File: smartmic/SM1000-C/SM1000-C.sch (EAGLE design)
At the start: 199 parts, among them CN1 HDR100-3, CN10 ST-3509, CN11 HDR100-3, CN12 DF11-16DS, CN2 MOLEX-MINI-B-SMT, CN3 RASM722PX, CN4 RJ-45, CN5 ST-3509, CN6 ST-3509, CN7 ST-3509, CN8 ST-3509, CN9 ST-3509, J1 JMP-2PIN, J3 JMP-2PIN, J4 JMP-2PIN, P1 TPAD50, P10 TPAD50, P11 TPAD50, P12 TPAD50, P13 TPAD50, P14 TPAD50, P15 TPAD50, P16 TPAD50, P17 TPAD50, P18 TPAD50, P19 TPAD50, P2 TPAD50, P20 TPAD50, P3 TPAD50, P4 TPAD50, P5 TPAD50, P6 TPAD50, P7 TPAD50, P8 TPAD50, P9 TPAD50, SW1 SW-BOURNS-7914S, SW2 SW-BOURNS-7914S, SW3 DPDT, SW4 SW-BOURNS-7914S, SW5 SW-BOURNS-7914J, T1 SM-LP-5001, T2 SM-LP-5001, U1 STM32F405, U2 LD3985M33R, U3 STMPS2141, U4 EMIF02-USB03F2, U5 TPS54329E, U6 LMV341, U7 LMV341, U8 LM386M-1, U9 LMV341

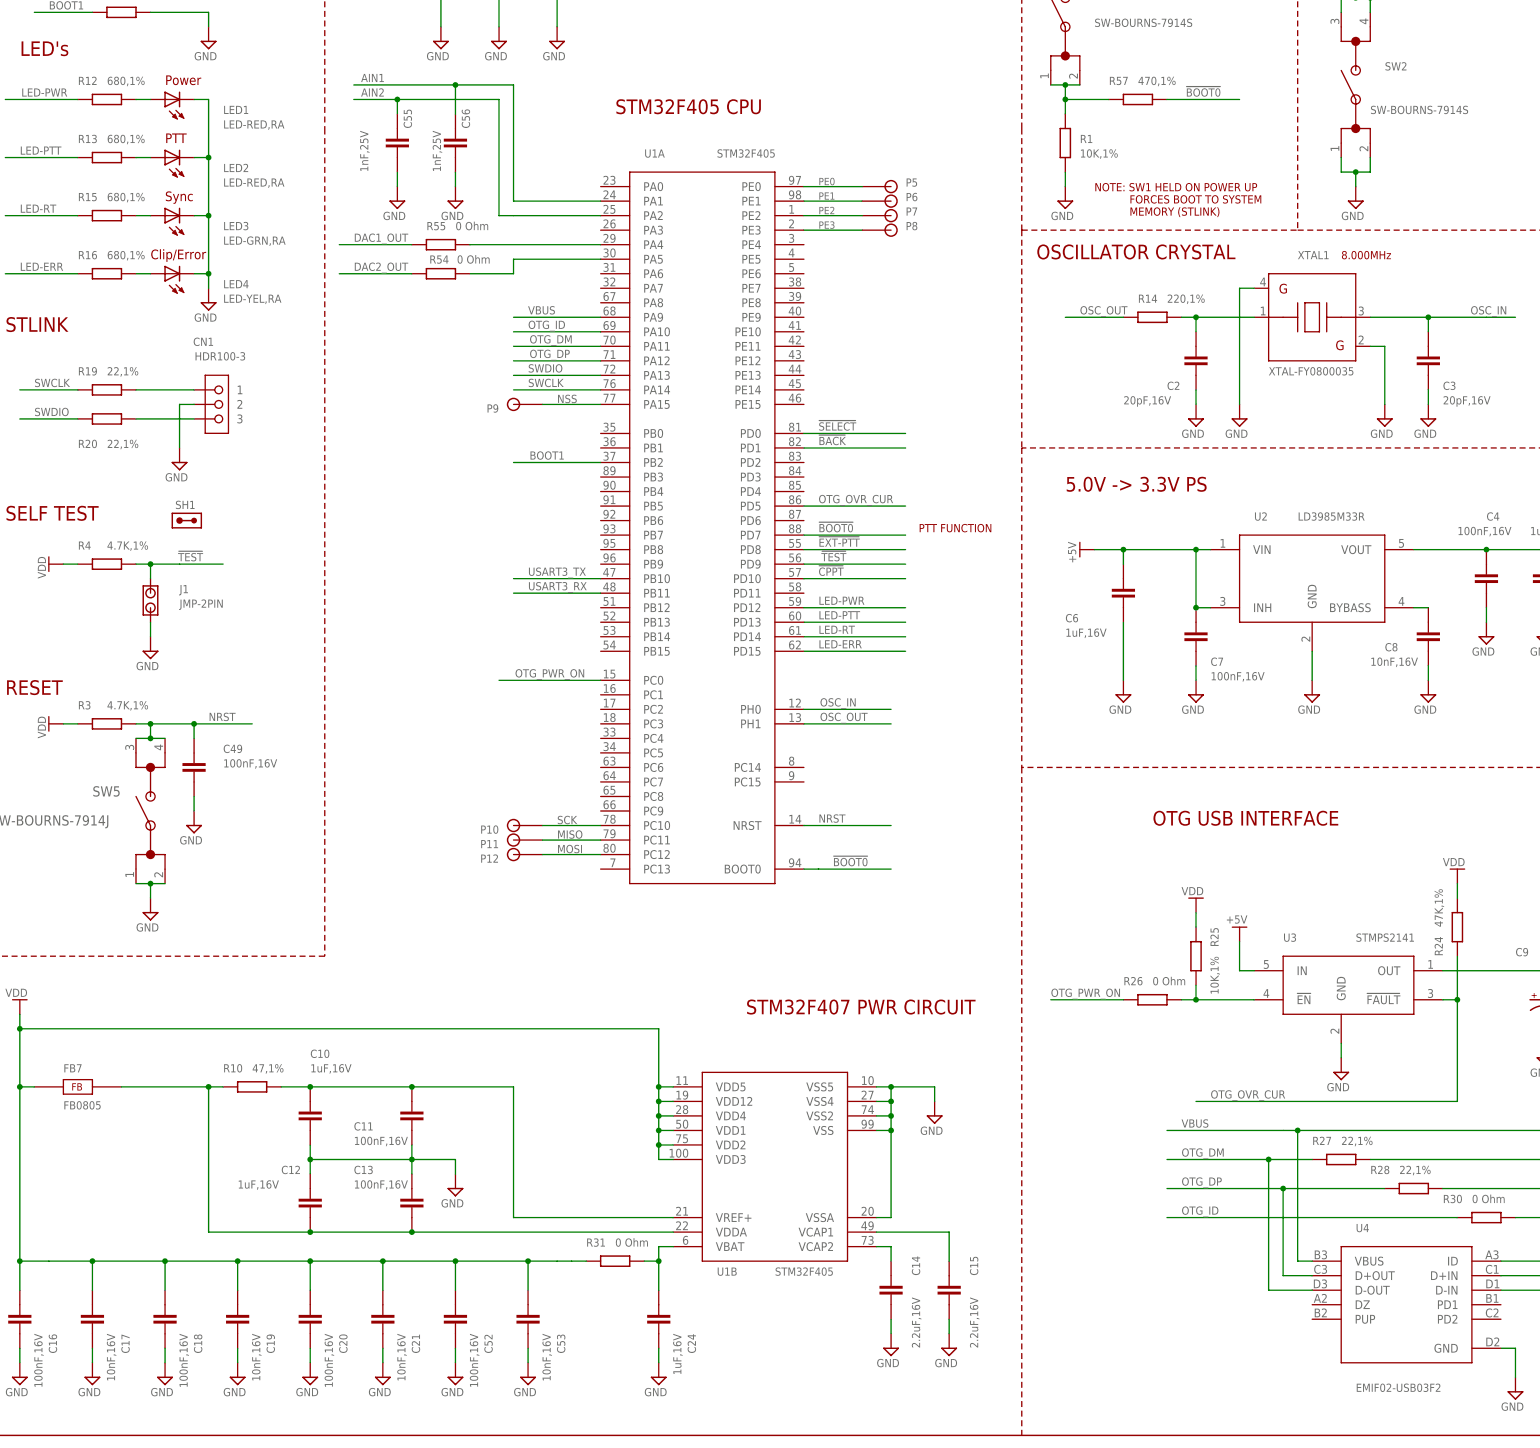
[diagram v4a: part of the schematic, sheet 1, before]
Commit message: Update schematics, PCB & BOM for addition of 0402 part footprints - RGB
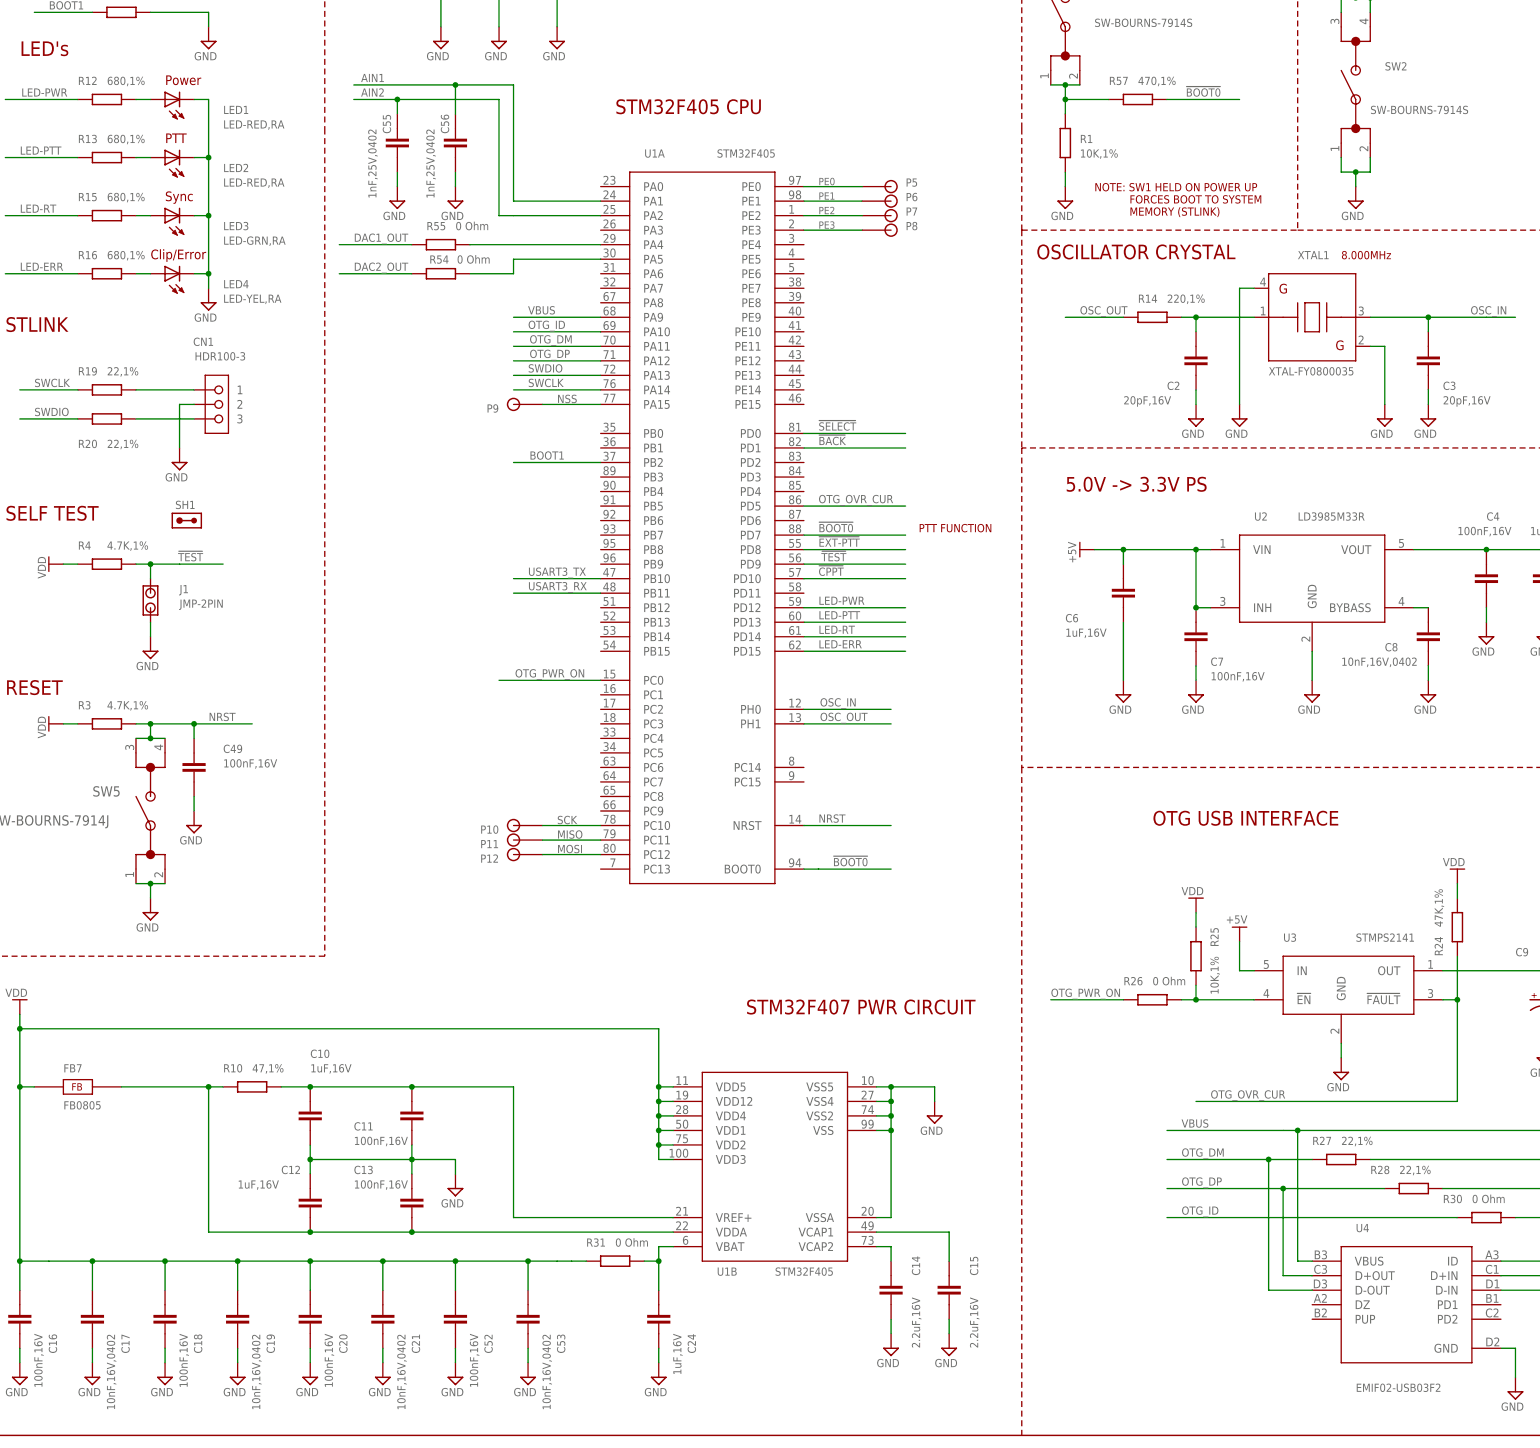
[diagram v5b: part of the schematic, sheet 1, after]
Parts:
- C1, C34, C55, C56: value 1nF,25V -> 1nF,25V,0402; device AA-ipc-7351-capacitor:CAPACITOR_0603 -> AA-ipc-7351-capacitor:CAPACITOR_0402
- C17, C19, C21, C53, C8: value 10nF,16V -> 10nF,16V,0402; device AA-ipc-7351-capacitor:CAPACITOR_0603 -> AA-ipc-7351-capacitor:CAPACITOR_0402
- C57: value 3.9nF,16V -> 3.9nF,16V,0402; device AA-ipc-7351-capacitor:CAPACITOR_0603 -> AA-ipc-7351-capacitor:CAPACITOR_0402
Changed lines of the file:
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@@
 <part name="V7" library="A-SUPPLY2" deviceset="GND" device=""/>
 <part name="V8" library="A-SUPPLY2" deviceset="GND" device=""/>
-<part name="C21" library="AA-ipc-7351-capacitor" deviceset="CAPACITOR_" device="0603" value="10nF,16V"/>
+<part name="C21" library="AA-ipc-7351-capacitor" deviceset="CAPACITOR_" device="0402" value="10nF,16V,0402"/>
 <part name="C20" library="AA-ipc-7351-capacitor" deviceset="CAPACITOR_" device="0603" value="100nF,16V"/>
-<part name="C19" library="AA-ipc-7351-capacitor" deviceset="CAPACITOR_" device="0603" value="10nF,16V"/>
+<part name="C19" library="AA-ipc-7351-capacitor" deviceset="CAPACITOR_" device="0402" value="10nF,16V,0402"/>
 <part name="C18" library="AA-ipc-7351-capacitor" deviceset="CAPACITOR_" device="0603" value="100nF,16V"/>
-<part name="C17" library="AA-ipc-7351-capacitor" deviceset="CAPACITOR_" device="0603" value="10nF,16V"/>
+<part name="C17" library="AA-ipc-7351-capacitor" deviceset="CAPACITOR_" device="0402" value="10nF,16V,0402"/>
 <part name="C16" library="AA-ipc-7351-capacitor" deviceset="CAPACITOR_" device="0603" value="100nF,16V"/>
 <part name="V9" library="A-SUPPLY2" deviceset="GND" device=""/>
@@
 <part name="V27" library="A-SUPPLY2" deviceset="+5V" device=""/>
 <part name="C5" library="AA-ipc-7351-capacitor" deviceset="CAPACITOR_" device="0603" value="1uF,16V"/>
-<part name="C8" library="AA-ipc-7351-capacitor" deviceset="CAPACITOR_" device="0603" value="10nF,16V"/>
+<part name="C8" library="AA-ipc-7351-capacitor" deviceset="CAPACITOR_" device="0402" value="10nF,16V,0402"/>
 <part name="C4" library="AA-ipc-7351-capacitor" deviceset="CAPACITOR_" device="0603" value="100nF,16V"/>
 <part name="V29" library="A-SUPPLY2" deviceset="GND" device=""/>
@@
 <part name="V55" library="A-SUPPLY2" deviceset="GND" device=""/>
 <part name="V56" library="A-SUPPLY2" deviceset="GND" device=""/>
-<part name="C34" library="AA-ipc-7351-capacitor" deviceset="CAPACITOR_" device="0603" value="1nF,25V"/>
+<part name="C34" library="AA-ipc-7351-capacitor" deviceset="CAPACITOR_" device="0402" value="1nF,25V,0402"/>
 <part name="R58" library="AA-ipc-7351-resistor" deviceset="RESISTOR_" device="0603" value="2.2K,1%"/>
 <part name="R40" library="AA-ipc-7351-resistor" deviceset="RESISTOR_" device="0603" value="2.2K,1%"/>
@@
 <part name="V71" library="A-SUPPLY2" deviceset="GND" device=""/>
 <part name="C52" library="AA-ipc-7351-capacitor" deviceset="CAPACITOR_" device="0603" value="100nF,16V"/>
-<part name="C53" library="AA-ipc-7351-capacitor" deviceset="CAPACITOR_" device="0603" value="10nF,16V"/>
+<part name="C53" library="AA-ipc-7351-capacitor" deviceset="CAPACITOR_" device="0402" value="10nF,16V,0402"/>
 <part name="V112" library="A-SUPPLY2" deviceset="GND" device=""/>
 <part name="V113" library="A-SUPPLY2" deviceset="GND" device=""/>
@@
 <part name="V123" library="A-SUPPLY2" deviceset="+5V" device=""/>
 <part name="U$3" library="A-SUPPLY2" deviceset="+VIN" device=""/>
-<part name="C1" library="AA-ipc-7351-capacitor" deviceset="CAPACITOR_" device="0603" value="1nF,25V"/>
+<part name="C1" library="AA-ipc-7351-capacitor" deviceset="CAPACITOR_" device="0402" value="1nF,25V,0402"/>
 <part name="V118" library="A-SUPPLY2" deviceset="GND" device=""/>
 <part name="C30" library="AA-ipc-7351-capacitor" deviceset="CAPACITOR_" device="0603" value="10nF,25V"/>
@@
 <part name="R55" library="AA-ipc-7351-resistor" deviceset="RESISTOR_" device="0805" value="0 Ohm"/>
 <part name="R54" library="AA-ipc-7351-resistor" deviceset="RESISTOR_" device="0805" value="0 Ohm"/>
-<part name="C55" library="AA-ipc-7351-capacitor" deviceset="CAPACITOR_" device="0603" value="1nF,25V"/>
-<part name="C56" library="AA-ipc-7351-capacitor" deviceset="CAPACITOR_" device="0603" value="1nF,25V"/>
+<part name="C55" library="AA-ipc-7351-capacitor" deviceset="CAPACITOR_" device="0402" value="1nF,25V,0402"/>
+<part name="C56" library="AA-ipc-7351-capacitor" deviceset="CAPACITOR_" device="0402" value="1nF,25V,0402"/>
 <part name="V125" library="A-SUPPLY2" deviceset="GND" device=""/>
 <part name="V126" library="A-SUPPLY2" deviceset="GND" device=""/>
@@
 <part name="V130" library="A-SUPPLY2" deviceset="GND" device=""/>
 <part name="R39" library="AA-ipc-7351-resistor" deviceset="RESISTOR_" device="1206" value="4.7,0.5W,1206"/>
-<part name="C57" library="AA-ipc-7351-capacitor" deviceset="CAPACITOR_" device="0603" value="3.9nF,16V"/>
+<part name="C57" library="AA-ipc-7351-capacitor" deviceset="CAPACITOR_" device="0402" value="3.9nF,16V,0402"/>
 <part name="V131" library="A-SUPPLY2" deviceset="GND" device=""/>
 <part name="R22" library="AA-ipc-7351-resistor" deviceset="RESISTOR_" device="0603" value="22.1K,1%"/>
@@
 <instance part="C8" gate="G$1" x="256.54" y="139.7" smashed="yes" rot="R270">
 <attribute name="NAME" x="248.92" y="137.16" size="1.4224" layer="95" ratio="9"/>
-<attribute name="VALUE" x="246.38" y="134.62" size="1.4224" layer="96" ratio="9"/>
+<attribute name="VALUE" x="241.3" y="134.62" size="1.4224" layer="96" ratio="9"/>
 </instance>
 <instance part="C4" gate="G$1" x="266.7" y="149.86" smashed="yes" rot="R270">
@@
 </instance>
 <instance part="C55" gate="G$1" x="76.2" y="226.06" smashed="yes" rot="R270">
-<attribute name="NAME" x="78.74" y="228.6" size="1.4224" layer="95" ratio="9" rot="R90"/>
-<attribute name="VALUE" x="71.12" y="220.98" size="1.4224" layer="96" ratio="9" rot="R90"/>
+<attribute name="NAME" x="73.66" y="231.14" size="1.4224" layer="95" ratio="9" rot="R270"/>
+<attribute name="VALUE" x="71.12" y="228.6" size="1.4224" layer="96" ratio="9" rot="R270"/>
 </instance>
 <instance part="C56" gate="G$1" x="86.36" y="226.06" smashed="yes" rot="R270">
-<attribute name="NAME" x="88.9" y="228.6" size="1.4224" layer="95" ratio="9" rot="R90"/>
-<attribute name="VALUE" x="83.82" y="220.98" size="1.4224" layer="96" ratio="9" rot="R90"/>
+<attribute name="NAME" x="83.82" y="231.14" size="1.4224" layer="95" ratio="9" rot="R270"/>
+<attribute name="VALUE" x="81.28" y="228.6" size="1.4224" layer="96" ratio="9" rot="R270"/>
 </instance>
 <instance part="V125" gate="GND" x="76.2" y="215.9"/>
@@
 <instance part="C1" gate="G$1" x="111.76" y="251.46" smashed="yes" rot="R90">
 <attribute name="NAME" x="106.68" y="246.38" size="1.4224" layer="95"/>
-<attribute name="VALUE" x="104.14" y="243.84" size="1.4224" layer="96"/>
+<attribute name="VALUE" x="99.06" y="243.84" size="1.4224" layer="96"/>
 </instance>
 <instance part="V118" gate="GND" x="111.76" y="241.3" smashed="yes">
